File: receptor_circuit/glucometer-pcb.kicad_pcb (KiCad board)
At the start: 2 copper layers, 257.7 x 161.4 mm, 252 parts

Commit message: added 3D models
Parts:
- removed the C1 at (40.3, 137.0)
- removed the C1 at (85.8, 43.6)
- removed the C1 at (84.8, 137.2)
- removed the C1 at (173.2, 138.0)
- removed the C1 at (216.4, 44.0)
- removed the C1 at (264.5, 137.5)
- removed the C1 at (129.8, 137.1)
- removed the C1 at (263.6, 44.1)
- removed the C1 at (173.2, 44.1)
- removed the C1 at (129.0, 43.6)
- removed the C1 at (216.2, 137.5)
- removed the C2 at (258.7, 44.1)
- removed the C2 at (168.3, 138.0)
- removed the C2 at (211.3, 137.5)
- removed the C2 at (124.1, 43.6)
- removed the C2 at (211.5, 44.0)
- removed the C2 at (35.4, 137.0)
- removed the C2 at (168.3, 44.1)
- removed the C2 at (124.9, 137.1)
- removed the C2 at (259.6, 137.5)
- removed the C2 at (80.9, 43.6)
- removed the C2 at (80.0, 137.2)
- removed the C3 at (207.9, 44.0)
- removed the C3 at (77.3, 43.6)
- removed the C3 at (31.8, 137.0)
- removed the C3 at (164.7, 138.0)
- removed the C3 at (255.9, 137.5)
- removed the C3 at (121.2, 137.1)
- removed the C3 at (255.0, 44.1)
- removed the C3 at (207.6, 137.5)
- removed the C3 at (76.3, 137.2)
- removed the C3 at (120.5, 43.6)
- removed the C3 at (164.7, 44.1)
- removed the GND1 at (202.3, 18.4)
- removed the GND1 at (202.1, 112.0)
- removed the GND1 at (70.7, 111.7)
- removed the GND1 at (249.5, 18.6)
- removed the GND1 at (71.7, 18.1)
- removed the GND1 at (115.7, 111.6)
- removed the GND1 at (159.1, 112.4)
- removed the GND1 at (250.3, 112.0)
- removed the GND1 at (159.1, 18.6)
- removed the GND1 at (114.9, 18.1)
- removed the GND1 at (26.2, 111.4)
- removed the LM1458N1 at (27.9, 139.1)
- removed the LM1458N1 at (116.6, 45.8)
- removed the LM1458N1 at (204.0, 46.1)
- removed the LM1458N1 at (203.8, 139.7)
- removed the LM1458N1 at (72.5, 139.4)
- removed the LM1458N1 at (73.4, 45.8)
- removed the LM1458N1 at (252.1, 139.7)
- removed the LM1458N1 at (160.8, 46.3)
- removed the LM1458N1 at (251.2, 46.3)
- removed the LM1458N1 at (117.4, 139.3)
- removed the LM1458N1 at (160.8, 140.1)
- removed the R1 at (44.3, 129.5)
- removed the R1 at (220.1, 130.1)
- removed the R1 at (89.8, 36.2)
- removed the R1 at (177.2, 36.7)
- removed the R1 at (132.9, 36.2)
- removed the R1 at (177.2, 130.5)
- removed the R1 at (267.5, 36.7)
- removed the R1 at (220.3, 36.6)
- removed the R1 at (88.8, 129.8)
- removed the R1 at (268.4, 130.1)
- removed the R1 at (133.7, 129.7)
- removed the R2 at (223.3, 44.2)
- removed the R2 at (135.9, 43.8)
- removed the R2 at (47.2, 137.2)
- removed the R2 at (270.4, 44.3)
- removed the R2 at (180.1, 138.2)
- removed the R2 at (180.1, 44.3)
- removed the R2 at (91.7, 137.4)
- removed the R2 at (271.3, 137.7)
- removed the R2 at (136.6, 137.3)
- removed the R2 at (92.7, 43.8)
- removed the R2 at (223.1, 137.7)
- removed the R3 at (168.4, 117.2)
- removed the R3 at (168.4, 23.3)
- removed the R3 at (35.5, 116.2)
- removed the R3 at (125.0, 116.4)
- removed the R3 at (211.4, 116.8)
- removed the R3 at (211.6, 23.2)
- removed the R3 at (258.8, 23.3)
- removed the R3 at (81.0, 22.8)
- removed the R3 at (259.7, 116.8)
- removed the R3 at (80.1, 116.4)
- removed the R3 at (124.2, 22.8)
- removed the R4 at (255.3, 31.0)
- removed the R4 at (208.1, 30.8)
- removed the R4 at (77.5, 30.5)
- removed the R4 at (164.9, 31.0)
- removed the R4 at (32.0, 123.8)
- removed the R4 at (256.2, 124.4)
- removed the R4 at (164.9, 124.8)
- removed the R4 at (121.5, 124.0)
- removed the R4 at (76.6, 124.0)
- removed the R4 at (120.7, 30.5)
- removed the R4 at (207.9, 124.4)
- removed the R5 at (46.4, 123.8)
- removed the R5 at (222.3, 124.4)
- removed the R5 at (179.3, 124.8)
- removed the R5 at (269.7, 31.0)
- removed the R5 at (270.6, 124.4)
- removed the R5 at (222.5, 30.9)
- removed the R5 at (91.9, 30.5)
- removed the R5 at (135.1, 30.5)
- removed the R5 at (179.3, 31.0)
- removed the R5 at (135.9, 124.0)
- removed the R5 at (91.0, 124.1)
- removed the R6 at (218.6, 116.8)
- removed the R6 at (132.2, 116.4)
- removed the R6 at (87.3, 116.5)
- removed the R6 at (266.0, 23.4)
- removed the R6 at (218.8, 23.2)
- removed the R6 at (266.9, 116.8)
- removed the R6 at (175.6, 117.2)
- removed the R6 at (175.6, 23.4)
- removed the R6 at (131.4, 22.9)
- removed the R6 at (88.2, 22.9)
- removed the R6 at (42.7, 116.2)
- removed the R7 at (128.5, 116.4)
- removed the R7 at (262.3, 23.4)
- removed the R7 at (172.0, 117.2)
- removed the R7 at (83.6, 116.5)
- removed the R7 at (263.2, 116.8)
- removed the R7 at (84.6, 22.9)
- removed the R7 at (39.1, 116.2)
- removed the R7 at (215.2, 23.2)
- removed the R7 at (172.0, 23.4)
- removed the R7 at (127.8, 22.9)
- removed the R7 at (215.0, 116.8)
- removed the RC4558IP1 at (247.4, 40.3)
- removed the RC4558IP1 at (200.2, 40.2)
- removed the RC4558IP1 at (248.3, 133.7)
- removed the RC4558IP1 at (200.0, 133.7)
- removed the RC4558IP1 at (68.7, 133.4)
- removed the RC4558IP1 at (69.6, 39.8)
- removed the RC4558IP1 at (24.1, 133.1)
- removed the RC4558IP1 at (113.6, 133.3)
- removed the RC4558IP1 at (112.8, 39.8)
- removed the RC4558IP1 at (157.0, 40.3)
- removed the RC4558IP1 at (157.0, 134.1)
- removed the RC4558IP2 at (200.2, 27.2)
- removed the RC4558IP2 at (248.3, 120.7)
- removed the RC4558IP2 at (112.8, 26.8)
- removed the RC4558IP2 at (157.1, 121.1)
- removed the RC4558IP2 at (68.7, 120.4)
- removed the RC4558IP2 at (69.7, 26.8)
- removed the RC4558IP2 at (247.4, 27.3)
- removed the RC4558IP2 at (24.2, 120.1)
- removed the RC4558IP2 at (113.6, 120.3)
- removed the RC4558IP2 at (157.1, 27.3)
- removed the RC4558IP2 at (200.0, 120.7)
- removed the RECEPTOR_DIODE1 at (123.9, 171.8)
- removed the RECEPTOR_DIODE1 at (34.4, 171.6)
- removed the RECEPTOR_DIODE1 at (210.5, 78.6)
- removed the RECEPTOR_DIODE1 at (210.3, 172.2)
- removed the RECEPTOR_DIODE1 at (78.9, 171.9)
- removed the RECEPTOR_DIODE1 at (167.3, 172.6)
- removed the RECEPTOR_DIODE1 at (123.1, 78.3)
- removed the RECEPTOR_DIODE1 at (257.6, 78.8)
- removed the RECEPTOR_DIODE1 at (258.5, 172.2)
- removed the RECEPTOR_DIODE1 at (79.9, 78.3)
- removed the RECEPTOR_DIODE1 at (167.3, 78.8)
- removed the REF** at (181.4, 173.7)
- removed the REF** at (224.6, 79.7)
- removed the REF** at (137.2, 79.4)
- removed the REF** at (243.5, 17.6)
- removed the REF** at (181.4, 111.5)
- removed the REF** at (65.8, 79.4)
- removed the REF** at (153.2, 173.7)
- removed the REF** at (64.8, 173.0)
- removed the REF** at (93.0, 173.0)
- removed the REF** at (272.6, 111.0)
- removed the REF** at (224.3, 173.3)
- removed the REF** at (272.6, 173.3)
- removed the REF** at (153.2, 79.9)
- removed the REF** at (196.2, 173.3)
- removed the REF** at (48.5, 110.5)
- removed the REF** at (243.5, 79.9)
- removed the REF** at (224.3, 111.0)
- removed the REF** at (224.5, 17.5)
- removed the REF** at (94.0, 17.1)
- removed the REF** at (196.4, 79.7)
- removed the REF** at (137.9, 110.6)
- removed the REF** at (109.7, 172.9)
- removed the REF** at (108.9, 17.1)
- removed the REF** at (153.1, 17.6)
- removed the REF** at (20.2, 110.4)
- removed the REF** at (153.1, 111.4)
- removed the REF** at (94.0, 79.4)
- removed the REF** at (271.7, 79.9)
- removed the REF** at (137.1, 17.1)
- removed the REF** at (20.3, 172.7)
- removed the REF** at (244.4, 173.3)
- removed the REF** at (137.9, 172.9)
- removed the REF** at (181.4, 79.9)
- removed the REF** at (244.4, 111.0)
- removed the REF** at (181.4, 17.6)
- removed the REF** at (109.0, 79.4)
- removed the REF** at (65.7, 17.1)
- removed the REF** at (109.7, 110.6)
- removed the REF** at (196.1, 111.0)
- removed the REF** at (196.3, 17.5)
- removed the REF** at (93.0, 110.7)
- removed the REF** at (64.8, 110.7)
- removed the REF** at (271.7, 17.6)
- removed the REF** at (48.5, 172.7)
- removed the S_OUT1 at (167.3, 18.6)
- removed the S_OUT1 at (258.6, 112.0)
- removed the S_OUT1 at (257.7, 18.6)
- removed the S_OUT1 at (167.3, 112.4)
- removed the S_OUT1 at (79.0, 111.7)
- removed the S_OUT1 at (123.1, 18.1)
- removed the S_OUT1 at (210.3, 112.0)
- removed the S_OUT1 at (34.4, 111.4)
- removed the S_OUT1 at (210.5, 18.4)
- removed the S_OUT1 at (79.9, 18.1)
- removed the S_OUT1 at (123.9, 111.6)
- removed the VCC1 at (175.6, 18.6)
- removed the VCC1 at (87.3, 111.7)
- removed the VCC1 at (42.7, 111.4)
- removed the VCC1 at (175.6, 112.4)
- removed the VCC1 at (266.9, 112.0)
- removed the VCC1 at (218.6, 112.0)
- removed the VCC1 at (218.8, 18.4)
- removed the VCC1 at (88.2, 18.1)
- removed the VCC1 at (131.4, 18.1)
- removed the VCC1 at (266.0, 18.6)
- removed the VCC1 at (132.2, 111.6)
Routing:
- net VCC: track 968.4 -> 80.7 mm
- net Net-(C1-Pad1): track 717.5 -> 59.8 mm
- net /PWD_1.65: track 537.7 -> 44.8 mm
- net /SIGNAL_2: track 528.9 -> 44.1 mm
- net Net-(R6-Pad1): track 501.6 -> 41.8 mm
- net /SIGNAL_1: track 466.1 -> 38.8 mm
- net Net-(C1-Pad2): track 363.6 -> 30.3 mm
- net Net-(R7-Pad1): track 200.7 -> 16.7 mm
- net Net-(R3-Pad2): track 200.2 -> 16.7 mm
- net Net-(C3-Pad1): track 121.8 -> 10.1 mm
- net unconnected-(LM1458N1-Pad6): track 1.64 -> 0.14 mm
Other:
- board size 257.7 x 161.4 mm -> 33.3 x 67.1 mm

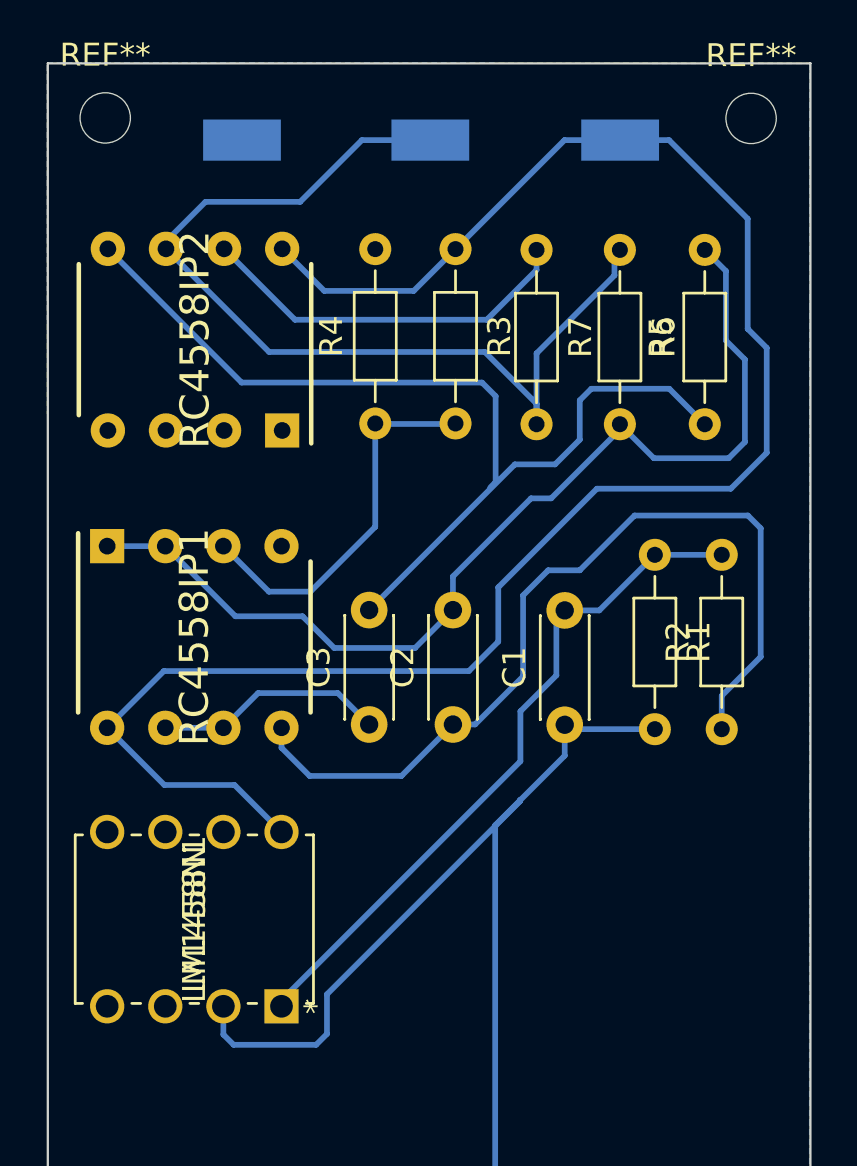
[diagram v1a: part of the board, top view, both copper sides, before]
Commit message: updated pcb pads
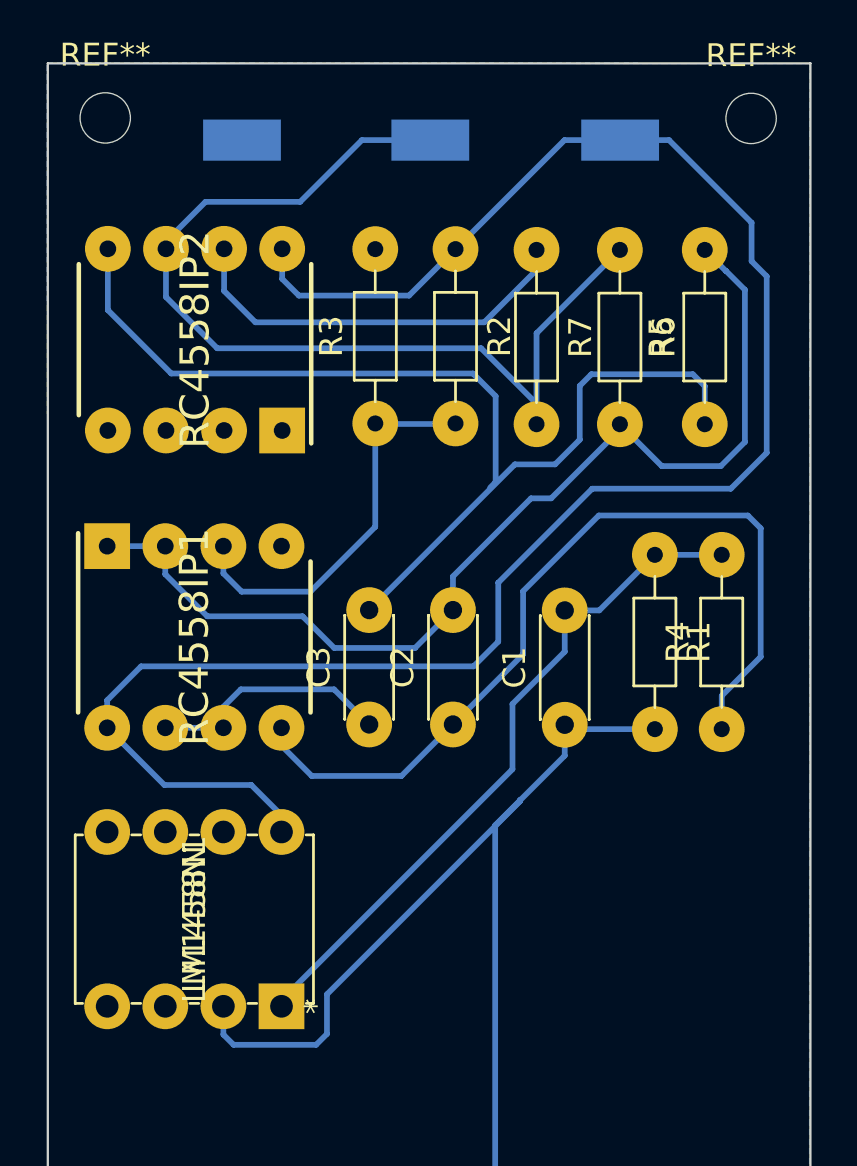
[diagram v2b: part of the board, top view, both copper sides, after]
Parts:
- C3: value 10u -> 1u
- R4: renamed from R2; value 330k -> 300k
- R5: value 25k -> 300k
- S_OUT1: value SIGNAL_OUT -> TestPoint
- renumbered R3 to R2, R4 to R3
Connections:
- net /PWD_1.65 renamed Net-(C2-Pad2)
- net /SIGNAL_1 renamed Net-(C2-Pad1)
- net /SIGNAL_2 renamed Net-(C3-Pad2)
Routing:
- net Net-(C3-Pad2): track 44.1 -> 47.5 mm
- net VCC: track 80.7 -> 82.9 mm
- net Net-(R6-Pad1): track 41.8 -> 43.1 mm
- net Net-(R7-Pad1): track 16.7 -> 17.9 mm
- net Net-(C2-Pad2): track 44.8 -> 45.8 mm
- net Net-(R2-Pad2): track 16.7 -> 17.4 mm
- net Net-(C3-Pad1): track 10.1 -> 10.8 mm
- net Net-(C2-Pad1): track 38.8 -> 38.3 mm

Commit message: added pdfs
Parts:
- added C1: 15p, Capacitor_THT:C_Disc_D4.3mm_W1.9mm_P5.00mm, F.Cu at (222.7, 44.8)
- added C1: 15p, Capacitor_THT:C_Disc_D4.3mm_W1.9mm_P5.00mm, F.Cu at (263.6, 121.0)
- added C1: 15p, Capacitor_THT:C_Disc_D4.3mm_W1.9mm_P5.00mm, F.Cu at (169.6, 44.8)
- added C1: 15p, Capacitor_THT:C_Disc_D4.3mm_W1.9mm_P5.00mm, F.Cu at (81.0, 43.6)
- added C1: 15p, Capacitor_THT:C_Disc_D4.3mm_W1.9mm_P5.00mm, F.Cu at (128.7, 121.0)
- added C1: 15p, Capacitor_THT:C_Disc_D4.3mm_W1.9mm_P5.00mm, F.Cu at (80.7, 123.5)
- added C1: 15p, Capacitor_THT:C_Disc_D4.3mm_W1.9mm_P5.00mm, F.Cu at (222.7, 121.0)
- added C1: 15p, Capacitor_THT:C_Disc_D4.3mm_W1.9mm_P5.00mm, F.Cu at (169.6, 121.0)
- added C1: 15p, Capacitor_THT:C_Disc_D4.3mm_W1.9mm_P5.00mm, F.Cu at (128.7, 44.8)
- added C1: 15p, Capacitor_THT:C_Disc_D4.3mm_W1.9mm_P5.00mm, F.Cu at (39.8, 123.5)
- added C1: 15p, Capacitor_THT:C_Disc_D4.3mm_W1.9mm_P5.00mm, F.Cu at (263.6, 44.8)
- added C2: 100n, Capacitor_THT:C_Disc_D4.3mm_W1.9mm_P5.00mm, F.Cu at (35.0, 123.5)
- added C2: 100n, Capacitor_THT:C_Disc_D4.3mm_W1.9mm_P5.00mm, F.Cu at (164.7, 44.8)
- added C2: 100n, Capacitor_THT:C_Disc_D4.3mm_W1.9mm_P5.00mm, F.Cu at (75.8, 123.5)
- added C2: 100n, Capacitor_THT:C_Disc_D4.3mm_W1.9mm_P5.00mm, F.Cu at (217.8, 121.0)
- added C2: 100n, Capacitor_THT:C_Disc_D4.3mm_W1.9mm_P5.00mm, F.Cu at (258.7, 121.0)
- added C2: 100n, Capacitor_THT:C_Disc_D4.3mm_W1.9mm_P5.00mm, F.Cu at (76.1, 43.6)
- added C2: 100n, Capacitor_THT:C_Disc_D4.3mm_W1.9mm_P5.00mm, F.Cu at (164.7, 121.0)
- added C2: 100n, Capacitor_THT:C_Disc_D4.3mm_W1.9mm_P5.00mm, F.Cu at (217.8, 44.8)
- added C2: 100n, Capacitor_THT:C_Disc_D4.3mm_W1.9mm_P5.00mm, F.Cu at (258.7, 44.8)
- added C2: 100n, Capacitor_THT:C_Disc_D4.3mm_W1.9mm_P5.00mm, F.Cu at (123.9, 44.8)
- added C2: 100n, Capacitor_THT:C_Disc_D4.3mm_W1.9mm_P5.00mm, F.Cu at (123.9, 121.0)
- added C3: 1u, Capacitor_THT:C_Disc_D4.3mm_W1.9mm_P5.00mm, F.Cu at (31.3, 123.5)
- added C3: 1u, Capacitor_THT:C_Disc_D4.3mm_W1.9mm_P5.00mm, F.Cu at (120.2, 44.8)
- added C3: 1u, Capacitor_THT:C_Disc_D4.3mm_W1.9mm_P5.00mm, F.Cu at (161.1, 121.0)
- added C3: 1u, Capacitor_THT:C_Disc_D4.3mm_W1.9mm_P5.00mm, F.Cu at (161.1, 44.8)
- added C3: 1u, Capacitor_THT:C_Disc_D4.3mm_W1.9mm_P5.00mm, F.Cu at (214.2, 121.0)
- added C3: 1u, Capacitor_THT:C_Disc_D4.3mm_W1.9mm_P5.00mm, F.Cu at (255.1, 44.8)
- added C3: 1u, Capacitor_THT:C_Disc_D4.3mm_W1.9mm_P5.00mm, F.Cu at (255.1, 121.0)
- added C3: 1u, Capacitor_THT:C_Disc_D4.3mm_W1.9mm_P5.00mm, F.Cu at (72.4, 43.6)
- added C3: 1u, Capacitor_THT:C_Disc_D4.3mm_W1.9mm_P5.00mm, F.Cu at (120.2, 121.0)
- added C3: 1u, Capacitor_THT:C_Disc_D4.3mm_W1.9mm_P5.00mm, F.Cu at (72.2, 123.5)
- added C3: 1u, Capacitor_THT:C_Disc_D4.3mm_W1.9mm_P5.00mm, F.Cu at (214.2, 44.8)
- added GND1: TestPoint, TestPoint:TestPoint_Keystone_5015_Micro-Minature, B.Cu at (155.5, 95.5)
- added GND1: TestPoint, TestPoint:TestPoint_Keystone_5015_Micro-Minature, B.Cu at (114.6, 19.3)
- added GND1: TestPoint, TestPoint:TestPoint_Keystone_5015_Micro-Minature, B.Cu at (249.5, 95.5)
- added GND1: TestPoint, TestPoint:TestPoint_Keystone_5015_Micro-Minature, B.Cu at (66.9, 18.1)
- added GND1: TestPoint, TestPoint:TestPoint_Keystone_5015_Micro-Minature, B.Cu at (114.6, 95.5)
- added GND1: TestPoint, TestPoint:TestPoint_Keystone_5015_Micro-Minature, B.Cu at (208.6, 95.5)
- added GND1: TestPoint, TestPoint:TestPoint_Keystone_5015_Micro-Minature, B.Cu at (25.7, 98.0)
- added GND1: TestPoint, TestPoint:TestPoint_Keystone_5015_Micro-Minature, B.Cu at (155.5, 19.3)
- added GND1: TestPoint, TestPoint:TestPoint_Keystone_5015_Micro-Minature, B.Cu at (249.5, 19.3)
- added GND1: TestPoint, TestPoint:TestPoint_Keystone_5015_Micro-Minature, B.Cu at (208.6, 19.3)
- added GND1: TestPoint, TestPoint:TestPoint_Keystone_5015_Micro-Minature, B.Cu at (66.6, 98.0)
- added LM1458N1: LM1458N, Custom:MC1458N, F.Cu at (251.2, 47.0)
- added LM1458N1: LM1458N, Custom:MC1458N, F.Cu at (210.3, 47.0)
- added LM1458N1: LM1458N, Custom:MC1458N, F.Cu at (68.6, 45.8)
- added LM1458N1: LM1458N, Custom:MC1458N, F.Cu at (157.3, 123.2)
- added LM1458N1: LM1458N, Custom:MC1458N, F.Cu at (116.4, 47.0)
- added LM1458N1: LM1458N, Custom:MC1458N, F.Cu at (68.4, 125.7)
- added LM1458N1: LM1458N, Custom:MC1458N, F.Cu at (157.3, 47.0)
- added LM1458N1: LM1458N, Custom:MC1458N, F.Cu at (116.4, 123.2)
- added LM1458N1: LM1458N, Custom:MC1458N, F.Cu at (27.5, 125.7)
- added LM1458N1: LM1458N, Custom:MC1458N, F.Cu at (210.3, 123.2)
- added LM1458N1: LM1458N, Custom:MC1458N, F.Cu at (251.2, 123.2)
- added R1: 100k, Resistor_THT:R_Axial_DIN0204_L3.6mm_D1.6mm_P7.62mm_Horizontal, F.Cu at (84.7, 116.1)
- added R1: 100k, Resistor_THT:R_Axial_DIN0204_L3.6mm_D1.6mm_P7.62mm_Horizontal, F.Cu at (173.6, 113.6)
- added R1: 100k, Resistor_THT:R_Axial_DIN0204_L3.6mm_D1.6mm_P7.62mm_Horizontal, F.Cu at (226.7, 37.4)
- added R1: 100k, Resistor_THT:R_Axial_DIN0204_L3.6mm_D1.6mm_P7.62mm_Horizontal, F.Cu at (132.7, 37.4)
- added R1: 100k, Resistor_THT:R_Axial_DIN0204_L3.6mm_D1.6mm_P7.62mm_Horizontal, F.Cu at (173.6, 37.4)
- added R1: 100k, Resistor_THT:R_Axial_DIN0204_L3.6mm_D1.6mm_P7.62mm_Horizontal, F.Cu at (226.7, 113.6)
- added R1: 100k, Resistor_THT:R_Axial_DIN0204_L3.6mm_D1.6mm_P7.62mm_Horizontal, F.Cu at (267.6, 37.4)
- added R1: 100k, Resistor_THT:R_Axial_DIN0204_L3.6mm_D1.6mm_P7.62mm_Horizontal, F.Cu at (132.7, 113.6)
- added R1: 100k, Resistor_THT:R_Axial_DIN0204_L3.6mm_D1.6mm_P7.62mm_Horizontal, F.Cu at (43.8, 116.1)
- added R1: 100k, Resistor_THT:R_Axial_DIN0204_L3.6mm_D1.6mm_P7.62mm_Horizontal, F.Cu at (267.6, 113.6)
- added R1: 100k, Resistor_THT:R_Axial_DIN0204_L3.6mm_D1.6mm_P7.62mm_Horizontal, F.Cu at (84.9, 36.2)
- added R2: 10k, Resistor_THT:R_Axial_DIN0204_L3.6mm_D1.6mm_P7.62mm_Horizontal, F.Cu at (76.0, 102.8)
- added R2: 10k, Resistor_THT:R_Axial_DIN0204_L3.6mm_D1.6mm_P7.62mm_Horizontal, F.Cu at (164.9, 24.0)
- added R2: 10k, Resistor_THT:R_Axial_DIN0204_L3.6mm_D1.6mm_P7.62mm_Horizontal, F.Cu at (124.0, 100.2)
- added R2: 10k, Resistor_THT:R_Axial_DIN0204_L3.6mm_D1.6mm_P7.62mm_Horizontal, F.Cu at (258.8, 24.0)
- added R2: 10k, Resistor_THT:R_Axial_DIN0204_L3.6mm_D1.6mm_P7.62mm_Horizontal, F.Cu at (218.0, 100.2)
- added R2: 10k, Resistor_THT:R_Axial_DIN0204_L3.6mm_D1.6mm_P7.62mm_Horizontal, F.Cu at (76.2, 22.8)
- added R2: 10k, Resistor_THT:R_Axial_DIN0204_L3.6mm_D1.6mm_P7.62mm_Horizontal, F.Cu at (218.0, 24.0)
- added R2: 10k, Resistor_THT:R_Axial_DIN0204_L3.6mm_D1.6mm_P7.62mm_Horizontal, F.Cu at (258.8, 100.2)
- added R2: 10k, Resistor_THT:R_Axial_DIN0204_L3.6mm_D1.6mm_P7.62mm_Horizontal, F.Cu at (124.0, 24.0)
- added R2: 10k, Resistor_THT:R_Axial_DIN0204_L3.6mm_D1.6mm_P7.62mm_Horizontal, F.Cu at (164.9, 100.2)
- added R2: 10k, Resistor_THT:R_Axial_DIN0204_L3.6mm_D1.6mm_P7.62mm_Horizontal, F.Cu at (35.1, 102.8)
- added R3: 10k, Resistor_THT:R_Axial_DIN0204_L3.6mm_D1.6mm_P7.62mm_Horizontal, F.Cu at (255.3, 107.8)
- added R3: 10k, Resistor_THT:R_Axial_DIN0204_L3.6mm_D1.6mm_P7.62mm_Horizontal, F.Cu at (72.5, 110.4)
- added R3: 10k, Resistor_THT:R_Axial_DIN0204_L3.6mm_D1.6mm_P7.62mm_Horizontal, F.Cu at (161.4, 31.6)
- added R3: 10k, Resistor_THT:R_Axial_DIN0204_L3.6mm_D1.6mm_P7.62mm_Horizontal, F.Cu at (255.3, 31.6)
- added R3: 10k, Resistor_THT:R_Axial_DIN0204_L3.6mm_D1.6mm_P7.62mm_Horizontal, F.Cu at (161.4, 107.8)
- added R3: 10k, Resistor_THT:R_Axial_DIN0204_L3.6mm_D1.6mm_P7.62mm_Horizontal, F.Cu at (72.7, 30.5)
- added R3: 10k, Resistor_THT:R_Axial_DIN0204_L3.6mm_D1.6mm_P7.62mm_Horizontal, F.Cu at (31.6, 110.4)
- added R3: 10k, Resistor_THT:R_Axial_DIN0204_L3.6mm_D1.6mm_P7.62mm_Horizontal, F.Cu at (120.5, 107.8)
- added R3: 10k, Resistor_THT:R_Axial_DIN0204_L3.6mm_D1.6mm_P7.62mm_Horizontal, F.Cu at (214.4, 107.8)
- added R3: 10k, Resistor_THT:R_Axial_DIN0204_L3.6mm_D1.6mm_P7.62mm_Horizontal, F.Cu at (214.4, 31.6)
- added R3: 10k, Resistor_THT:R_Axial_DIN0204_L3.6mm_D1.6mm_P7.62mm_Horizontal, F.Cu at (120.5, 31.6)
- added R4: 300k, Resistor_THT:R_Axial_DIN0204_L3.6mm_D1.6mm_P7.62mm_Horizontal, F.Cu at (229.6, 121.2)
- added R4: 300k, Resistor_THT:R_Axial_DIN0204_L3.6mm_D1.6mm_P7.62mm_Horizontal, F.Cu at (135.6, 121.2)
- added R4: 300k, Resistor_THT:R_Axial_DIN0204_L3.6mm_D1.6mm_P7.62mm_Horizontal, F.Cu at (87.6, 123.7)
- added R4: 300k, Resistor_THT:R_Axial_DIN0204_L3.6mm_D1.6mm_P7.62mm_Horizontal, F.Cu at (135.6, 45.0)
- added R4: 300k, Resistor_THT:R_Axial_DIN0204_L3.6mm_D1.6mm_P7.62mm_Horizontal, F.Cu at (176.5, 45.0)
- added R4: 300k, Resistor_THT:R_Axial_DIN0204_L3.6mm_D1.6mm_P7.62mm_Horizontal, F.Cu at (176.5, 121.2)
- added R4: 300k, Resistor_THT:R_Axial_DIN0204_L3.6mm_D1.6mm_P7.62mm_Horizontal, F.Cu at (270.5, 121.2)
- added R4: 300k, Resistor_THT:R_Axial_DIN0204_L3.6mm_D1.6mm_P7.62mm_Horizontal, F.Cu at (229.6, 45.0)
- added R4: 300k, Resistor_THT:R_Axial_DIN0204_L3.6mm_D1.6mm_P7.62mm_Horizontal, F.Cu at (46.7, 123.7)
- added R4: 300k, Resistor_THT:R_Axial_DIN0204_L3.6mm_D1.6mm_P7.62mm_Horizontal, F.Cu at (270.5, 45.0)
- added R4: 300k, Resistor_THT:R_Axial_DIN0204_L3.6mm_D1.6mm_P7.62mm_Horizontal, F.Cu at (87.9, 43.8)
- added R5: 300k, Resistor_THT:R_Axial_DIN0204_L3.6mm_D1.6mm_P7.62mm_Horizontal, F.Cu at (46.0, 110.4)
- added R5: 300k, Resistor_THT:R_Axial_DIN0204_L3.6mm_D1.6mm_P7.62mm_Horizontal, F.Cu at (228.8, 107.9)
- added R5: 300k, Resistor_THT:R_Axial_DIN0204_L3.6mm_D1.6mm_P7.62mm_Horizontal, F.Cu at (134.9, 107.9)
- added R5: 300k, Resistor_THT:R_Axial_DIN0204_L3.6mm_D1.6mm_P7.62mm_Horizontal, F.Cu at (228.8, 31.7)
- added R5: 300k, Resistor_THT:R_Axial_DIN0204_L3.6mm_D1.6mm_P7.62mm_Horizontal, F.Cu at (134.9, 31.7)
- added R5: 300k, Resistor_THT:R_Axial_DIN0204_L3.6mm_D1.6mm_P7.62mm_Horizontal, F.Cu at (269.7, 31.7)
- added R5: 300k, Resistor_THT:R_Axial_DIN0204_L3.6mm_D1.6mm_P7.62mm_Horizontal, F.Cu at (269.7, 107.9)
- added R5: 300k, Resistor_THT:R_Axial_DIN0204_L3.6mm_D1.6mm_P7.62mm_Horizontal, F.Cu at (175.8, 31.7)
- added R5: 300k, Resistor_THT:R_Axial_DIN0204_L3.6mm_D1.6mm_P7.62mm_Horizontal, F.Cu at (86.9, 110.4)
- added R5: 300k, Resistor_THT:R_Axial_DIN0204_L3.6mm_D1.6mm_P7.62mm_Horizontal, F.Cu at (87.1, 30.5)
- added R5: 300k, Resistor_THT:R_Axial_DIN0204_L3.6mm_D1.6mm_P7.62mm_Horizontal, F.Cu at (175.8, 107.9)
- added R6: 1k, Resistor_THT:R_Axial_DIN0204_L3.6mm_D1.6mm_P7.62mm_Horizontal, F.Cu at (266.0, 100.3)
- added R6: 1k, Resistor_THT:R_Axial_DIN0204_L3.6mm_D1.6mm_P7.62mm_Horizontal, F.Cu at (83.4, 22.9)
- added R6: 1k, Resistor_THT:R_Axial_DIN0204_L3.6mm_D1.6mm_P7.62mm_Horizontal, F.Cu at (42.3, 102.8)
- added R6: 1k, Resistor_THT:R_Axial_DIN0204_L3.6mm_D1.6mm_P7.62mm_Horizontal, F.Cu at (225.1, 100.2)
- added R6: 1k, Resistor_THT:R_Axial_DIN0204_L3.6mm_D1.6mm_P7.62mm_Horizontal, F.Cu at (225.1, 24.0)
- added R6: 1k, Resistor_THT:R_Axial_DIN0204_L3.6mm_D1.6mm_P7.62mm_Horizontal, F.Cu at (83.1, 102.8)
- added R6: 1k, Resistor_THT:R_Axial_DIN0204_L3.6mm_D1.6mm_P7.62mm_Horizontal, F.Cu at (131.2, 100.2)
- added R6: 1k, Resistor_THT:R_Axial_DIN0204_L3.6mm_D1.6mm_P7.62mm_Horizontal, F.Cu at (131.2, 24.0)
- added R6: 1k, Resistor_THT:R_Axial_DIN0204_L3.6mm_D1.6mm_P7.62mm_Horizontal, F.Cu at (266.0, 24.1)
- added R6: 1k, Resistor_THT:R_Axial_DIN0204_L3.6mm_D1.6mm_P7.62mm_Horizontal, F.Cu at (172.0, 24.1)
- added R6: 1k, Resistor_THT:R_Axial_DIN0204_L3.6mm_D1.6mm_P7.62mm_Horizontal, F.Cu at (172.0, 100.3)
- added R7: 100k, Resistor_THT:R_Axial_DIN0204_L3.6mm_D1.6mm_P7.62mm_Horizontal, F.Cu at (168.4, 100.3)
- added R7: 100k, Resistor_THT:R_Axial_DIN0204_L3.6mm_D1.6mm_P7.62mm_Horizontal, F.Cu at (221.5, 100.2)
- added R7: 100k, Resistor_THT:R_Axial_DIN0204_L3.6mm_D1.6mm_P7.62mm_Horizontal, F.Cu at (262.4, 100.3)
- added R7: 100k, Resistor_THT:R_Axial_DIN0204_L3.6mm_D1.6mm_P7.62mm_Horizontal, F.Cu at (79.5, 102.8)
- added R7: 100k, Resistor_THT:R_Axial_DIN0204_L3.6mm_D1.6mm_P7.62mm_Horizontal, F.Cu at (221.5, 24.0)
- added R7: 100k, Resistor_THT:R_Axial_DIN0204_L3.6mm_D1.6mm_P7.62mm_Horizontal, F.Cu at (127.5, 24.0)
- added R7: 100k, Resistor_THT:R_Axial_DIN0204_L3.6mm_D1.6mm_P7.62mm_Horizontal, F.Cu at (262.4, 24.1)
- added R7: 100k, Resistor_THT:R_Axial_DIN0204_L3.6mm_D1.6mm_P7.62mm_Horizontal, F.Cu at (38.6, 102.8)
- added R7: 100k, Resistor_THT:R_Axial_DIN0204_L3.6mm_D1.6mm_P7.62mm_Horizontal, F.Cu at (168.4, 24.1)
- added R7: 100k, Resistor_THT:R_Axial_DIN0204_L3.6mm_D1.6mm_P7.62mm_Horizontal, F.Cu at (127.5, 100.2)
- added R7: 100k, Resistor_THT:R_Axial_DIN0204_L3.6mm_D1.6mm_P7.62mm_Horizontal, F.Cu at (79.8, 22.9)
- added RC4558IP1: RC4558IP, Custom:DIP794W53P254L959H508Q8N, F.Cu at (247.4, 117.2)
- added RC4558IP1: RC4558IP, Custom:DIP794W53P254L959H508Q8N, F.Cu at (64.8, 39.8)
- added RC4558IP1: RC4558IP, Custom:DIP794W53P254L959H508Q8N, F.Cu at (23.7, 119.7)
- added RC4558IP1: RC4558IP, Custom:DIP794W53P254L959H508Q8N, F.Cu at (153.4, 41.0)
- added RC4558IP1: RC4558IP, Custom:DIP794W53P254L959H508Q8N, F.Cu at (206.5, 41.0)
- added RC4558IP1: RC4558IP, Custom:DIP794W53P254L959H508Q8N, F.Cu at (112.6, 41.0)
- added RC4558IP1: RC4558IP, Custom:DIP794W53P254L959H508Q8N, F.Cu at (247.4, 41.0)
- added RC4558IP1: RC4558IP, Custom:DIP794W53P254L959H508Q8N, F.Cu at (64.5, 119.7)
- added RC4558IP1: RC4558IP, Custom:DIP794W53P254L959H508Q8N, F.Cu at (112.6, 117.2)
- added RC4558IP1: RC4558IP, Custom:DIP794W53P254L959H508Q8N, F.Cu at (206.5, 117.2)
- added RC4558IP1: RC4558IP, Custom:DIP794W53P254L959H508Q8N, F.Cu at (153.4, 117.2)
- added RC4558IP2: RC4558IP, Custom:DIP794W53P254L959H508Q8N, F.Cu at (153.5, 28.0)
- added RC4558IP2: RC4558IP, Custom:DIP794W53P254L959H508Q8N, F.Cu at (206.6, 104.2)
- added RC4558IP2: RC4558IP, Custom:DIP794W53P254L959H508Q8N, F.Cu at (112.6, 28.0)
- added RC4558IP2: RC4558IP, Custom:DIP794W53P254L959H508Q8N, F.Cu at (153.5, 104.2)
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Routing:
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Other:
- board size 33.3 x 67.1 mm -> 257.1 x 147 mm

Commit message: updated PCBs
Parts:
- removed the C1 at (222.7, 44.8)
- removed the C1 at (263.6, 121.0)
- removed the C1 at (169.6, 44.8)
- removed the C1 at (81.0, 43.6)
- removed the C1 at (128.7, 121.0)
- removed the C1 at (80.7, 123.5)
- removed the C1 at (222.7, 121.0)
- removed the C1 at (169.6, 121.0)
- removed the C1 at (128.7, 44.8)
- removed the C1 at (39.8, 123.5)
- removed the C1 at (263.6, 44.8)
- removed the C2 at (35.0, 123.5)
- removed the C2 at (164.7, 44.8)
- removed the C2 at (75.8, 123.5)
- removed the C2 at (217.8, 121.0)
- removed the C2 at (258.7, 121.0)
- removed the C2 at (76.1, 43.6)
- removed the C2 at (164.7, 121.0)
- removed the C2 at (217.8, 44.8)
- removed the C2 at (258.7, 44.8)
- removed the C2 at (123.9, 44.8)
- removed the C2 at (123.9, 121.0)
- removed the C3 at (31.3, 123.5)
- removed the C3 at (120.2, 44.8)
- removed the C3 at (161.1, 121.0)
- removed the C3 at (161.1, 44.8)
- removed the C3 at (214.2, 121.0)
- removed the C3 at (255.1, 44.8)
- removed the C3 at (255.1, 121.0)
- removed the C3 at (72.4, 43.6)
- removed the C3 at (120.2, 121.0)
- removed the C3 at (72.2, 123.5)
- removed the C3 at (214.2, 44.8)
- removed the GND1 at (155.5, 95.5)
- removed the GND1 at (114.6, 19.3)
- removed the GND1 at (249.5, 95.5)
- removed the GND1 at (66.9, 18.1)
- removed the GND1 at (114.6, 95.5)
- removed the GND1 at (208.6, 95.5)
- removed the GND1 at (25.7, 98.0)
- removed the GND1 at (155.5, 19.3)
- removed the GND1 at (249.5, 19.3)
- removed the GND1 at (208.6, 19.3)
- removed the GND1 at (66.6, 98.0)
- removed the LM1458N1 at (251.2, 47.0)
- removed the LM1458N1 at (210.3, 47.0)
- removed the LM1458N1 at (68.6, 45.8)
- removed the LM1458N1 at (157.3, 123.2)
- removed the LM1458N1 at (116.4, 47.0)
- removed the LM1458N1 at (68.4, 125.7)
- removed the LM1458N1 at (157.3, 47.0)
- removed the LM1458N1 at (116.4, 123.2)
- removed the LM1458N1 at (27.5, 125.7)
- removed the LM1458N1 at (210.3, 123.2)
- removed the LM1458N1 at (251.2, 123.2)
- removed the R1 at (84.7, 116.1)
- removed the R1 at (173.6, 113.6)
- removed the R1 at (226.7, 37.4)
- removed the R1 at (132.7, 37.4)
- removed the R1 at (173.6, 37.4)
- removed the R1 at (226.7, 113.6)
- removed the R1 at (267.6, 37.4)
- removed the R1 at (132.7, 113.6)
- removed the R1 at (43.8, 116.1)
- removed the R1 at (267.6, 113.6)
- removed the R1 at (84.9, 36.2)
- removed the R2 at (76.0, 102.8)
- removed the R2 at (164.9, 24.0)
- removed the R2 at (124.0, 100.2)
- removed the R2 at (258.8, 24.0)
- removed the R2 at (218.0, 100.2)
- removed the R2 at (76.2, 22.8)
- removed the R2 at (218.0, 24.0)
- removed the R2 at (258.8, 100.2)
- removed the R2 at (124.0, 24.0)
- removed the R2 at (164.9, 100.2)
- removed the R2 at (35.1, 102.8)
- removed the R3 at (255.3, 107.8)
- removed the R3 at (72.5, 110.4)
- removed the R3 at (161.4, 31.6)
- removed the R3 at (255.3, 31.6)
- removed the R3 at (161.4, 107.8)
- removed the R3 at (72.7, 30.5)
- removed the R3 at (31.6, 110.4)
- removed the R3 at (120.5, 107.8)
- removed the R3 at (214.4, 107.8)
- removed the R3 at (214.4, 31.6)
- removed the R3 at (120.5, 31.6)
- removed the R4 at (229.6, 121.2)
- removed the R4 at (135.6, 121.2)
- removed the R4 at (87.6, 123.7)
- removed the R4 at (135.6, 45.0)
- removed the R4 at (176.5, 45.0)
- removed the R4 at (176.5, 121.2)
- removed the R4 at (270.5, 121.2)
- removed the R4 at (229.6, 45.0)
- removed the R4 at (46.7, 123.7)
- removed the R4 at (270.5, 45.0)
- removed the R4 at (87.9, 43.8)
- removed the R5 at (46.0, 110.4)
- removed the R5 at (228.8, 107.9)
- removed the R5 at (134.9, 107.9)
- removed the R5 at (228.8, 31.7)
- removed the R5 at (134.9, 31.7)
- removed the R5 at (269.7, 31.7)
- removed the R5 at (269.7, 107.9)
- removed the R5 at (175.8, 31.7)
- removed the R5 at (86.9, 110.4)
- removed the R5 at (87.1, 30.5)
- removed the R5 at (175.8, 107.9)
- removed the R6 at (266.0, 100.3)
- removed the R6 at (83.4, 22.9)
- removed the R6 at (42.3, 102.8)
- removed the R6 at (225.1, 100.2)
- removed the R6 at (225.1, 24.0)
- removed the R6 at (83.1, 102.8)
- removed the R6 at (131.2, 100.2)
- removed the R6 at (131.2, 24.0)
- removed the R6 at (266.0, 24.1)
- removed the R6 at (172.0, 24.1)
- removed the R6 at (172.0, 100.3)
- removed the R7 at (168.4, 100.3)
- removed the R7 at (221.5, 100.2)
- removed the R7 at (262.4, 100.3)
- removed the R7 at (79.5, 102.8)
- removed the R7 at (221.5, 24.0)
- removed the R7 at (127.5, 24.0)
- removed the R7 at (262.4, 24.1)
- removed the R7 at (38.6, 102.8)
- removed the R7 at (168.4, 24.1)
- removed the R7 at (127.5, 100.2)
- removed the R7 at (79.8, 22.9)
- removed the RC4558IP1 at (247.4, 117.2)
- removed the RC4558IP1 at (64.8, 39.8)
- removed the RC4558IP1 at (23.7, 119.7)
- removed the RC4558IP1 at (153.4, 41.0)
- removed the RC4558IP1 at (206.5, 41.0)
- removed the RC4558IP1 at (112.6, 41.0)
- removed the RC4558IP1 at (247.4, 41.0)
- removed the RC4558IP1 at (64.5, 119.7)
- removed the RC4558IP1 at (112.6, 117.2)
- removed the RC4558IP1 at (206.5, 117.2)
- removed the RC4558IP1 at (153.4, 117.2)
- removed the RC4558IP2 at (153.5, 28.0)
- removed the RC4558IP2 at (206.6, 104.2)
- removed the RC4558IP2 at (112.6, 28.0)
- removed the RC4558IP2 at (153.5, 104.2)
- removed the RC4558IP2 at (206.6, 28.0)
- removed the RC4558IP2 at (64.8, 26.8)
- removed the RC4558IP2 at (247.5, 28.0)
- removed the RC4558IP2 at (64.6, 106.7)
- removed the RC4558IP2 at (247.5, 104.2)
- removed the RC4558IP2 at (112.6, 104.2)
- removed the RC4558IP2 at (23.7, 106.7)
- removed the RECEPTOR_DIODE1 at (257.7, 155.6)
- removed the RECEPTOR_DIODE1 at (122.8, 79.4)
- removed the RECEPTOR_DIODE1 at (257.7, 79.4)
- removed the RECEPTOR_DIODE1 at (216.8, 79.4)
- removed the RECEPTOR_DIODE1 at (75.1, 78.3)
- removed the RECEPTOR_DIODE1 at (163.7, 155.6)
- removed the RECEPTOR_DIODE1 at (216.8, 155.6)
- removed the RECEPTOR_DIODE1 at (33.9, 158.2)
- removed the RECEPTOR_DIODE1 at (122.8, 155.6)
- removed the RECEPTOR_DIODE1 at (74.8, 158.2)
- removed the RECEPTOR_DIODE1 at (163.7, 79.4)
- removed the REF** at (136.9, 156.7)
- removed the REF** at (149.6, 80.6)
- removed the REF** at (177.8, 156.7)
- removed the REF** at (177.8, 18.3)
- removed the REF** at (108.7, 18.3)
- removed the REF** at (19.8, 159.3)
- removed the REF** at (230.9, 156.7)
- removed the REF** at (19.8, 97.0)
- removed the REF** at (271.8, 156.7)
- removed the REF** at (48.0, 159.3)
- removed the REF** at (202.6, 94.5)
- removed the REF** at (177.8, 80.5)
- removed the REF** at (136.9, 80.5)
- removed the REF** at (149.6, 156.8)
- removed the REF** at (60.9, 17.1)
- removed the REF** at (48.0, 97.0)
- removed the REF** at (89.1, 79.4)
- removed the REF** at (108.7, 156.8)
- removed the REF** at (136.9, 94.5)
- removed the REF** at (60.7, 159.3)
- removed the REF** at (149.5, 94.5)
- removed the REF** at (230.9, 94.5)
- removed the REF** at (136.9, 18.3)
- removed the REF** at (243.5, 94.5)
- removed the REF** at (243.6, 80.6)
- removed the REF** at (243.5, 18.3)
- removed the REF** at (202.6, 18.3)
- removed the REF** at (202.7, 80.6)
- removed the REF** at (60.6, 97.0)
- removed the REF** at (177.8, 94.5)
- removed the REF** at (61.0, 79.4)
- removed the REF** at (230.9, 80.5)
- removed the REF** at (88.9, 97.0)
- removed the REF** at (271.8, 80.5)
- removed the REF** at (149.5, 18.3)
- removed the REF** at (89.1, 17.1)
- removed the REF** at (271.8, 94.5)
- removed the REF** at (108.7, 80.6)
- removed the REF** at (202.7, 156.8)
- removed the REF** at (271.8, 18.3)
- removed the REF** at (88.9, 159.3)
- removed the REF** at (108.7, 94.5)
- removed the REF** at (230.9, 18.3)
- removed the REF** at (243.6, 156.8)
- removed the S_OUT1 at (163.8, 19.3)
- removed the S_OUT1 at (257.7, 95.5)
- removed the S_OUT1 at (122.9, 19.3)
- removed the S_OUT1 at (216.8, 19.3)
- removed the S_OUT1 at (257.7, 19.3)
- removed the S_OUT1 at (75.1, 18.1)
- removed the S_OUT1 at (122.9, 95.5)
- removed the S_OUT1 at (74.9, 98.0)
- removed the S_OUT1 at (216.8, 95.5)
- removed the S_OUT1 at (34.0, 98.0)
- removed the S_OUT1 at (163.8, 95.5)
- removed the VCC1 at (266.0, 95.5)
- removed the VCC1 at (225.1, 95.5)
- removed the VCC1 at (83.4, 18.1)
- removed the VCC1 at (131.2, 19.3)
- removed the VCC1 at (266.0, 19.3)
- removed the VCC1 at (42.3, 98.0)
- removed the VCC1 at (83.2, 98.0)
- removed the VCC1 at (225.1, 19.3)
- removed the VCC1 at (172.1, 19.3)
- removed the VCC1 at (131.2, 95.5)
- removed the VCC1 at (172.1, 95.5)
- added C1: 15p, Capacitor_THT:C_Disc_D4.3mm_W1.9mm_P5.00mm, F.Cu at (131.8, 140.3)
- added C1: 15p, Capacitor_THT:C_Disc_D4.3mm_W1.9mm_P5.00mm, F.Cu at (264.7, 60.1)
- added C1: 15p, Capacitor_THT:C_Disc_D4.3mm_W1.9mm_P5.00mm, F.Cu at (262.7, 140.0)
- added C1: 15p, Capacitor_THT:C_Disc_D4.3mm_W1.9mm_P5.00mm, F.Cu at (219.3, 62.9)
- added C1: 15p, Capacitor_THT:C_Disc_D4.3mm_W1.9mm_P5.00mm, F.Cu at (84.3, 140.5)
- added C1: 15p, Capacitor_THT:C_Disc_D4.3mm_W1.9mm_P5.00mm, F.Cu at (41.1, 140.4)
- added C1: 15p, Capacitor_THT:C_Disc_D4.3mm_W1.9mm_P5.00mm, F.Cu at (130.4, 60.2)
- added C1: 15p, Capacitor_THT:C_Disc_D4.3mm_W1.9mm_P5.00mm, F.Cu at (178.9, 139.8)
- added C1: 15p, Capacitor_THT:C_Disc_D4.3mm_W1.9mm_P5.00mm, F.Cu at (220.7, 140.3)
- added C1: 15p, Capacitor_THT:C_Disc_D4.3mm_W1.9mm_P5.00mm, F.Cu at (87.2, 59.0)
- added C1: 15p, Capacitor_THT:C_Disc_D4.3mm_W1.9mm_P5.00mm, F.Cu at (172.2, 61.8)
- added C2: 100n, Capacitor_THT:C_Disc_D4.3mm_W1.9mm_P5.00mm, F.Cu at (79.4, 140.5)
- added C2: 100n, Capacitor_THT:C_Disc_D4.3mm_W1.9mm_P5.00mm, F.Cu at (259.8, 60.1)
- added C2: 100n, Capacitor_THT:C_Disc_D4.3mm_W1.9mm_P5.00mm, F.Cu at (214.4, 62.9)
- added C2: 100n, Capacitor_THT:C_Disc_D4.3mm_W1.9mm_P5.00mm, F.Cu at (82.3, 59.0)
- added C2: 100n, Capacitor_THT:C_Disc_D4.3mm_W1.9mm_P5.00mm, F.Cu at (167.3, 61.8)
- added C2: 100n, Capacitor_THT:C_Disc_D4.3mm_W1.9mm_P5.00mm, F.Cu at (125.5, 60.1)
- added C2: 100n, Capacitor_THT:C_Disc_D4.3mm_W1.9mm_P5.00mm, F.Cu at (36.3, 140.4)
- added C2: 100n, Capacitor_THT:C_Disc_D4.3mm_W1.9mm_P5.00mm, F.Cu at (174.0, 139.7)
- added C2: 100n, Capacitor_THT:C_Disc_D4.3mm_W1.9mm_P5.00mm, F.Cu at (257.8, 140.0)
- added C2: 100n, Capacitor_THT:C_Disc_D4.3mm_W1.9mm_P5.00mm, F.Cu at (126.9, 140.3)
- added C2: 100n, Capacitor_THT:C_Disc_D4.3mm_W1.9mm_P5.00mm, F.Cu at (215.8, 140.3)
- added C3: 1u, Capacitor_THT:C_Disc_D4.3mm_W1.9mm_P5.00mm, F.Cu at (123.2, 140.3)
- added C3: 1u, Capacitor_THT:C_Disc_D4.3mm_W1.9mm_P5.00mm, F.Cu at (254.2, 140.0)
- added C3: 1u, Capacitor_THT:C_Disc_D4.3mm_W1.9mm_P5.00mm, F.Cu at (256.1, 60.1)
- added C3: 1u, Capacitor_THT:C_Disc_D4.3mm_W1.9mm_P5.00mm, F.Cu at (75.8, 140.5)
- added C3: 1u, Capacitor_THT:C_Disc_D4.3mm_W1.9mm_P5.00mm, F.Cu at (212.1, 140.3)
- added C3: 1u, Capacitor_THT:C_Disc_D4.3mm_W1.9mm_P5.00mm, F.Cu at (170.3, 139.7)
- added C3: 1u, Capacitor_THT:C_Disc_D4.3mm_W1.9mm_P5.00mm, F.Cu at (210.7, 62.9)
- added C3: 1u, Capacitor_THT:C_Disc_D4.3mm_W1.9mm_P5.00mm, F.Cu at (32.6, 140.4)
- added C3: 1u, Capacitor_THT:C_Disc_D4.3mm_W1.9mm_P5.00mm, F.Cu at (78.6, 59.0)
- added C3: 1u, Capacitor_THT:C_Disc_D4.3mm_W1.9mm_P5.00mm, F.Cu at (163.6, 61.8)
- added C3: 1u, Capacitor_THT:C_Disc_D4.3mm_W1.9mm_P5.00mm, F.Cu at (121.8, 60.1)
- added GND1: TestPoint, TestPoint:TestPoint_Keystone_5015_Micro-Minature, B.Cu at (205.2, 37.3)
- added GND1: TestPoint, TestPoint:TestPoint_Keystone_5015_Micro-Minature, B.Cu at (27.0, 114.8)
- added GND1: TestPoint, TestPoint:TestPoint_Keystone_5015_Micro-Minature, B.Cu at (248.6, 114.4)
- added GND1: TestPoint, TestPoint:TestPoint_Keystone_5015_Micro-Minature, B.Cu at (206.6, 114.8)
- added GND1: TestPoint, TestPoint:TestPoint_Keystone_5015_Micro-Minature, B.Cu at (70.2, 115.0)
- added GND1: TestPoint, TestPoint:TestPoint_Keystone_5015_Micro-Minature, B.Cu at (117.7, 114.8)
- added GND1: TestPoint, TestPoint:TestPoint_Keystone_5015_Micro-Minature, B.Cu at (158.1, 36.2)
- added GND1: TestPoint, TestPoint:TestPoint_Keystone_5015_Micro-Minature, B.Cu at (250.6, 34.6)
- added GND1: TestPoint, TestPoint:TestPoint_Keystone_5015_Micro-Minature, B.Cu at (116.3, 34.6)
- added GND1: TestPoint, TestPoint:TestPoint_Keystone_5015_Micro-Minature, B.Cu at (73.1, 33.5)
- added GND1: TestPoint, TestPoint:TestPoint_Keystone_5015_Micro-Minature, B.Cu at (164.8, 114.2)
- added LM1458N1: LM1458N, Custom:MC1458N, F.Cu at (206.9, 65.0)
- added LM1458N1: LM1458N, Custom:MC1458N, F.Cu at (166.5, 141.9)
- added LM1458N1: LM1458N, Custom:MC1458N, F.Cu at (118.0, 62.3)
- added LM1458N1: LM1458N, Custom:MC1458N, F.Cu at (71.9, 142.7)
- added LM1458N1: LM1458N, Custom:MC1458N, F.Cu at (252.3, 62.3)
- added LM1458N1: LM1458N, Custom:MC1458N, F.Cu at (208.3, 142.5)
- added LM1458N1: LM1458N, Custom:MC1458N, F.Cu at (74.8, 61.2)
- added LM1458N1: LM1458N, Custom:MC1458N, F.Cu at (159.8, 63.9)
- added LM1458N1: LM1458N, Custom:MC1458N, F.Cu at (250.3, 142.1)
- added LM1458N1: LM1458N, Custom:MC1458N, F.Cu at (28.8, 142.5)
- added LM1458N1: LM1458N, Custom:MC1458N, F.Cu at (119.4, 142.5)
- added R1: 100k, Resistor_THT:R_Axial_DIN0204_L3.6mm_D1.6mm_P7.62mm_Horizontal, F.Cu at (88.3, 133.1)
- added R1: 100k, Resistor_THT:R_Axial_DIN0204_L3.6mm_D1.6mm_P7.62mm_Horizontal, F.Cu at (134.3, 52.7)
- added R1: 100k, Resistor_THT:R_Axial_DIN0204_L3.6mm_D1.6mm_P7.62mm_Horizontal, F.Cu at (224.6, 132.9)
- added R1: 100k, Resistor_THT:R_Axial_DIN0204_L3.6mm_D1.6mm_P7.62mm_Horizontal, F.Cu at (182.8, 132.3)
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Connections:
- R7 pad 1: Net-(R7-Pad1) -> Net-(RC4558IP2-Pad7)
- RC4558IP2 pad 7: Net-(R7-Pad1) -> Net-(RC4558IP2-Pad7)
- S_OUT1 pad 1: Net-(R6-Pad1) -> Net-(RC4558IP2-Pad7)
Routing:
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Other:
- board size 257.1 x 147 mm -> 256.9 x 148.5 mm
- board text added: "R4k4210 & KremoWy"
